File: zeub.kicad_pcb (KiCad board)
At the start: 2 copper layers, 94.5 x 62.2 mm, 227 parts, among them J1 debug-port, J2 OLED-128x64, J3 USB_C_Receptacle_USB2.0, Q1 AO3401A, Q2 AO3401A, Q3 AO3401A, Q4 AO3401A, SW1 SKRHA, SW2 RotaryEncoder_Switch, U1 IS31FL3729, U10 LTC4054ES5-4.2, U2 IS31FL3729, U3 IS31FL3729, U4 IS31FL3729, U5 holyiot-18010-no-underside, U6 MT25QL128ABA1ESE, U7 MC78M05_TO252, U8 XC6206PxxxMR, U9 SRV05-4

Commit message: routed RGB
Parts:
- moved D1 20.6 mm to (95.0, 20.0)
- moved D10 20.6 mm to (100.0, 25.0)
- moved D100 20.6 mm to (155.0, 35.0)
- moved D101 20.6 mm to (155.0, 40.0)
- moved D102 20.6 mm to (155.0, 45.0)
- moved D103 20.6 mm to (155.0, 50.0)
- moved D104 20.6 mm to (155.0, 55.0)
- moved D105 20.6 mm to (160.0, 20.0)
- moved D106 20.6 mm to (160.0, 25.0)
- moved D107 20.6 mm to (160.0, 30.0)
- moved D108 20.6 mm to (160.0, 35.0)
- moved D109 20.6 mm to (160.0, 40.0)
- moved D11 20.6 mm to (100.0, 30.0)
- moved D110 20.6 mm to (160.0, 45.0)
- moved D111 20.6 mm to (160.0, 50.0)
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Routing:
- net /led/RGB_G7: track 0.00 -> 44.7 mm, vias 0 -> 8
- net /led/RGB_G6: track 0.00 -> 44.7 mm, vias 0 -> 8
- net /led/RGB_G5: track 0.00 -> 44.7 mm, vias 0 -> 8
- net /led/RGB_G4: track 0.00 -> 44.7 mm, vias 0 -> 8
- net /led/RGB_G3: track 0.00 -> 44.7 mm, vias 0 -> 8
- net /led/RGB_G2: track 0.00 -> 44.7 mm, vias 0 -> 8
- net /led/RGB_G1: track 0.00 -> 44.7 mm, vias 0 -> 8
- net /led/RGB_G0: track 0.00 -> 44.7 mm, vias 0 -> 8
- net /led/RGB_C7: track 0.00 -> 44.2 mm
- net /led/RGB_C6: track 0.00 -> 44.2 mm
- net /led/RGB_C5: track 0.00 -> 44.2 mm
- net /led/RGB_C4: track 0.00 -> 44.2 mm
- net /led/RGB_C3: track 0.00 -> 44.2 mm
- net /led/RGB_C2: track 0.00 -> 44.2 mm
- net /led/RGB_C1: track 0.00 -> 44.2 mm
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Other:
- board outline removed

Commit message: routed matrix + PWM driver
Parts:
- added D197: white, Diode_SMD:D_0603_1608Metric, F.Cu at (128.0, 16.0)
- added D198: white, Diode_SMD:D_0603_1608Metric, F.Cu at (128.0, 20.0)
- added D199: white, Diode_SMD:D_0603_1608Metric, F.Cu at (128.0, 24.0)
- added D200: white, Diode_SMD:D_0603_1608Metric, F.Cu at (128.0, 28.0)
- added D201: white, Diode_SMD:D_0603_1608Metric, F.Cu at (132.0, 0.00)
- added D202: white, Diode_SMD:D_0603_1608Metric, F.Cu at (132.0, 4.00)
- added D203: white, Diode_SMD:D_0603_1608Metric, F.Cu at (132.0, 8.00)
- added D204: white, Diode_SMD:D_0603_1608Metric, F.Cu at (132.0, 12.0)
- added D205: white, Diode_SMD:D_0603_1608Metric, F.Cu at (132.0, 16.0)
- added D206: white, Diode_SMD:D_0603_1608Metric, F.Cu at (132.0, 20.0)
- added D207: white, Diode_SMD:D_0603_1608Metric, F.Cu at (132.0, 24.0)
- added D208: white, Diode_SMD:D_0603_1608Metric, F.Cu at (132.0, 28.0)
- added D209: white, Diode_SMD:D_0603_1608Metric, F.Cu at (136.0, 0.00)
- added D210: white, Diode_SMD:D_0603_1608Metric, F.Cu at (136.0, 4.00)
- added D211: white, Diode_SMD:D_0603_1608Metric, F.Cu at (136.0, 8.00)
- added D212: white, Diode_SMD:D_0603_1608Metric, F.Cu at (136.0, 12.0)
- added D213: white, Diode_SMD:D_0603_1608Metric, F.Cu at (136.0, 16.0)
- added D214: white, Diode_SMD:D_0603_1608Metric, F.Cu at (136.0, 20.0)
- added D215: white, Diode_SMD:D_0603_1608Metric, F.Cu at (136.0, 24.0)
- added D216: white, Diode_SMD:D_0603_1608Metric, F.Cu at (136.0, 28.0)
- added D217: white, Diode_SMD:D_0603_1608Metric, F.Cu at (140.0, 0.00)
- added D218: white, Diode_SMD:D_0603_1608Metric, F.Cu at (140.0, 4.00)
- added D219: white, Diode_SMD:D_0603_1608Metric, F.Cu at (140.0, 8.00)
- added D220: white, Diode_SMD:D_0603_1608Metric, F.Cu at (140.0, 12.0)
- added D221: white, Diode_SMD:D_0603_1608Metric, F.Cu at (140.0, 16.0)
- added D222: white, Diode_SMD:D_0603_1608Metric, F.Cu at (140.0, 20.0)
- added D223: white, Diode_SMD:D_0603_1608Metric, F.Cu at (140.0, 24.0)
- added D224: white, Diode_SMD:D_0603_1608Metric, F.Cu at (140.0, 28.0)
- added D225: white, Diode_SMD:D_0603_1608Metric, F.Cu at (144.0, 0.00)
- added D226: white, Diode_SMD:D_0603_1608Metric, F.Cu at (144.0, 4.00)
- added D227: white, Diode_SMD:D_0603_1608Metric, F.Cu at (144.0, 8.00)
- added D228: white, Diode_SMD:D_0603_1608Metric, F.Cu at (144.0, 12.0)
- added D229: white, Diode_SMD:D_0603_1608Metric, F.Cu at (144.0, 16.0)
- added D230: white, Diode_SMD:D_0603_1608Metric, F.Cu at (144.0, 20.0)
- added D231: white, Diode_SMD:D_0603_1608Metric, F.Cu at (144.0, 24.0)
- added D232: white, Diode_SMD:D_0603_1608Metric, F.Cu at (144.0, 28.0)
- added D233: white, Diode_SMD:D_0603_1608Metric, F.Cu at (148.0, 0.00)
- added D234: white, Diode_SMD:D_0603_1608Metric, F.Cu at (148.0, 4.00)
- added D235: white, Diode_SMD:D_0603_1608Metric, F.Cu at (148.0, 8.00)
- added D236: white, Diode_SMD:D_0603_1608Metric, F.Cu at (148.0, 12.0)
- added D237: white, Diode_SMD:D_0603_1608Metric, F.Cu at (148.0, 16.0)
- added D238: white, Diode_SMD:D_0603_1608Metric, F.Cu at (148.0, 20.0)
- added D239: white, Diode_SMD:D_0603_1608Metric, F.Cu at (148.0, 24.0)
- added D240: white, Diode_SMD:D_0603_1608Metric, F.Cu at (148.0, 28.0)
- added D241: white, Diode_SMD:D_0603_1608Metric, F.Cu at (152.0, 0.00)
- added D242: white, Diode_SMD:D_0603_1608Metric, F.Cu at (152.0, 4.00)
- added D243: white, Diode_SMD:D_0603_1608Metric, F.Cu at (152.0, 8.00)
- added D244: white, Diode_SMD:D_0603_1608Metric, F.Cu at (152.0, 12.0)
- added D245: white, Diode_SMD:D_0603_1608Metric, F.Cu at (152.0, 16.0)
- added D246: white, Diode_SMD:D_0603_1608Metric, F.Cu at (152.0, 20.0)
- added D247: white, Diode_SMD:D_0603_1608Metric, F.Cu at (152.0, 24.0)
- added D248: white, Diode_SMD:D_0603_1608Metric, F.Cu at (152.0, 28.0)
- added D249: white, Diode_SMD:D_0603_1608Metric, F.Cu at (156.0, 0.00)
- added D250: white, Diode_SMD:D_0603_1608Metric, F.Cu at (156.0, 4.00)
- added D251: white, Diode_SMD:D_0603_1608Metric, F.Cu at (156.0, 8.00)
- added D252: white, Diode_SMD:D_0603_1608Metric, F.Cu at (156.0, 12.0)
- added D253: white, Diode_SMD:D_0603_1608Metric, F.Cu at (156.0, 16.0)
- added D254: white, Diode_SMD:D_0603_1608Metric, F.Cu at (156.0, 20.0)
- added D255: white, Diode_SMD:D_0603_1608Metric, F.Cu at (156.0, 24.0)
- added D256: white, Diode_SMD:D_0603_1608Metric, F.Cu at (156.0, 28.0)
- added D257: LED_RABG, LED_SMD:LED_ASMB-KTF0-0A306, F.Cu at (0.00, 0.00)
- added D258: LED_RABG, LED_SMD:LED_ASMB-KTF0-0A306, F.Cu at (0.00, 4.00)
- added D259: LED_RABG, LED_SMD:LED_ASMB-KTF0-0A306, F.Cu at (0.00, 8.00)
- added D260: LED_RABG, LED_SMD:LED_ASMB-KTF0-0A306, F.Cu at (0.00, 12.0)
- added D261: LED_RABG, LED_SMD:LED_ASMB-KTF0-0A306, F.Cu at (0.00, 16.0)
- added D262: LED_RABG, LED_SMD:LED_ASMB-KTF0-0A306, F.Cu at (0.00, 20.0)
- added D263: LED_RABG, LED_SMD:LED_ASMB-KTF0-0A306, F.Cu at (0.00, 24.0)
- added D264: LED_RABG, LED_SMD:LED_ASMB-KTF0-0A306, F.Cu at (0.00, 28.0)
- added D265: LED_RABG, LED_SMD:LED_ASMB-KTF0-0A306, F.Cu at (4.00, 0.00)
- added D266: LED_RABG, LED_SMD:LED_ASMB-KTF0-0A306, F.Cu at (4.00, 4.00)
- added D267: LED_RABG, LED_SMD:LED_ASMB-KTF0-0A306, F.Cu at (4.00, 8.00)
- added D268: LED_RABG, LED_SMD:LED_ASMB-KTF0-0A306, F.Cu at (4.00, 12.0)
- added D269: LED_RABG, LED_SMD:LED_ASMB-KTF0-0A306, F.Cu at (4.00, 16.0)
- added D270: LED_RABG, LED_SMD:LED_ASMB-KTF0-0A306, F.Cu at (4.00, 20.0)
- added D271: LED_RABG, LED_SMD:LED_ASMB-KTF0-0A306, F.Cu at (4.00, 24.0)
- added D272: LED_RABG, LED_SMD:LED_ASMB-KTF0-0A306, F.Cu at (4.00, 28.0)
- added D273: LED_RABG, LED_SMD:LED_ASMB-KTF0-0A306, F.Cu at (8.00, 0.00)
- added D274: LED_RABG, LED_SMD:LED_ASMB-KTF0-0A306, F.Cu at (8.00, 4.00)
- added D275: LED_RABG, LED_SMD:LED_ASMB-KTF0-0A306, F.Cu at (8.00, 8.00)
- added D276: LED_RABG, LED_SMD:LED_ASMB-KTF0-0A306, F.Cu at (8.00, 12.0)
- added D277: LED_RABG, LED_SMD:LED_ASMB-KTF0-0A306, F.Cu at (8.00, 16.0)
- added D278: LED_RABG, LED_SMD:LED_ASMB-KTF0-0A306, F.Cu at (8.00, 20.0)
- added D279: LED_RABG, LED_SMD:LED_ASMB-KTF0-0A306, F.Cu at (8.00, 24.0)
- added D280: LED_RABG, LED_SMD:LED_ASMB-KTF0-0A306, F.Cu at (8.00, 28.0)
- added D281: LED_RABG, LED_SMD:LED_ASMB-KTF0-0A306, F.Cu at (12.0, 0.00)
- added D282: LED_RABG, LED_SMD:LED_ASMB-KTF0-0A306, F.Cu at (12.0, 4.00)
- added D283: LED_RABG, LED_SMD:LED_ASMB-KTF0-0A306, F.Cu at (12.0, 8.00)
- added D284: LED_RABG, LED_SMD:LED_ASMB-KTF0-0A306, F.Cu at (12.0, 12.0)
- added D285: LED_RABG, LED_SMD:LED_ASMB-KTF0-0A306, F.Cu at (12.0, 16.0)
- added D286: LED_RABG, LED_SMD:LED_ASMB-KTF0-0A306, F.Cu at (12.0, 20.0)
- added D287: LED_RABG, LED_SMD:LED_ASMB-KTF0-0A306, F.Cu at (12.0, 24.0)
- added D288: LED_RABG, LED_SMD:LED_ASMB-KTF0-0A306, F.Cu at (12.0, 28.0)
- added D289: LED_RABG, LED_SMD:LED_ASMB-KTF0-0A306, F.Cu at (16.0, 0.00)
- added D290: LED_RABG, LED_SMD:LED_ASMB-KTF0-0A306, F.Cu at (16.0, 4.00)
- added D291: LED_RABG, LED_SMD:LED_ASMB-KTF0-0A306, F.Cu at (16.0, 8.00)
- added D292: LED_RABG, LED_SMD:LED_ASMB-KTF0-0A306, F.Cu at (16.0, 12.0)
- added D293: LED_RABG, LED_SMD:LED_ASMB-KTF0-0A306, F.Cu at (16.0, 16.0)
- added D294: LED_RABG, LED_SMD:LED_ASMB-KTF0-0A306, F.Cu at (16.0, 20.0)
- added D295: LED_RABG, LED_SMD:LED_ASMB-KTF0-0A306, F.Cu at (16.0, 24.0)
- added D296: LED_RABG, LED_SMD:LED_ASMB-KTF0-0A306, F.Cu at (16.0, 28.0)
- added D297: LED_RABG, LED_SMD:LED_ASMB-KTF0-0A306, F.Cu at (20.0, 0.00)
- added D298: LED_RABG, LED_SMD:LED_ASMB-KTF0-0A306, F.Cu at (20.0, 4.00)
- added D299: LED_RABG, LED_SMD:LED_ASMB-KTF0-0A306, F.Cu at (20.0, 8.00)
- added D300: LED_RABG, LED_SMD:LED_ASMB-KTF0-0A306, F.Cu at (20.0, 12.0)
- added D301: LED_RABG, LED_SMD:LED_ASMB-KTF0-0A306, F.Cu at (20.0, 16.0)
- added D302: LED_RABG, LED_SMD:LED_ASMB-KTF0-0A306, F.Cu at (20.0, 20.0)
- added D303: LED_RABG, LED_SMD:LED_ASMB-KTF0-0A306, F.Cu at (20.0, 24.0)
- added D304: LED_RABG, LED_SMD:LED_ASMB-KTF0-0A306, F.Cu at (20.0, 28.0)
- added D305: LED_RABG, LED_SMD:LED_ASMB-KTF0-0A306, F.Cu at (24.0, 0.00)
- added D306: LED_RABG, LED_SMD:LED_ASMB-KTF0-0A306, F.Cu at (24.0, 4.00)
- added D307: LED_RABG, LED_SMD:LED_ASMB-KTF0-0A306, F.Cu at (24.0, 8.00)
- added D308: LED_RABG, LED_SMD:LED_ASMB-KTF0-0A306, F.Cu at (24.0, 12.0)
- added D309: LED_RABG, LED_SMD:LED_ASMB-KTF0-0A306, F.Cu at (24.0, 16.0)
- added D310: LED_RABG, LED_SMD:LED_ASMB-KTF0-0A306, F.Cu at (24.0, 20.0)
- added D311: LED_RABG, LED_SMD:LED_ASMB-KTF0-0A306, F.Cu at (24.0, 24.0)
- added D312: LED_RABG, LED_SMD:LED_ASMB-KTF0-0A306, F.Cu at (24.0, 28.0)
- added D313: LED_RABG, LED_SMD:LED_ASMB-KTF0-0A306, F.Cu at (28.0, 0.00)
- added D314: LED_RABG, LED_SMD:LED_ASMB-KTF0-0A306, F.Cu at (28.0, 4.00)
- added D315: LED_RABG, LED_SMD:LED_ASMB-KTF0-0A306, F.Cu at (28.0, 8.00)
- added D316: LED_RABG, LED_SMD:LED_ASMB-KTF0-0A306, F.Cu at (28.0, 12.0)
- added D317: LED_RABG, LED_SMD:LED_ASMB-KTF0-0A306, F.Cu at (28.0, 16.0)
- added D318: LED_RABG, LED_SMD:LED_ASMB-KTF0-0A306, F.Cu at (28.0, 20.0)
- added D319: LED_RABG, LED_SMD:LED_ASMB-KTF0-0A306, F.Cu at (28.0, 24.0)
- added D320: LED_RABG, LED_SMD:LED_ASMB-KTF0-0A306, F.Cu at (28.0, 28.0)
- added D321: D_Schottky, Diode_SMD:D_SOD-123, B.Cu at (-19.0, 58.8)
- added D322: D_Schottky, Diode_SMD:D_SOD-123, B.Cu at (-13.2, 62.1)
- added D323: D_Schottky, Diode_SMD:D_SOD-123, B.Cu at (-13.2, 58.8)
- added D324: LED, Diode_SMD:D_0805_2012Metric, B.Cu at (-18.4, 61.9)
- added J4: Barrel_Jack_Switch, Connector_BarrelJack:BarrelJack_CUI_PJ-102AH_Horizontal, B.Cu at (-5.05, 3.50)
- added J5: Conn_01x03, Connector_PinHeader_2.54mm:PinHeader_1x03_P2.54mm_Vertical, F.Cu at (-16.8, 21.7)
- added J6: Conn_01x03, Connector_PinHeader_2.54mm:PinHeader_1x03_P2.54mm_Vertical, F.Cu at (-16.8, 11.7)
- added Q5: AO3401A, Package_TO_SOT_SMD:SOT-23, B.Cu at (-33.5, 49.2)
- added R13: 10k, Resistor_SMD:R_0603_1608Metric, B.Cu at (55.0, 39.2)
- added R14: 10k, Resistor_SMD:R_0603_1608Metric, B.Cu at (116.7, 45.5)
- added R15: 10k, Resistor_SMD:R_0603_1608Metric, B.Cu at (3.50, 38.0)
- added R16: 10k, Resistor_SMD:R_0603_1608Metric, B.Cu at (20.2, 40.0)
- added R17: 20, Resistor_SMD:R_0603_1608Metric, F.Cu at (31.5, 31.2)
- added R18: 20, Resistor_SMD:R_0603_1608Metric, F.Cu at (35.2, 31.2)
- added R19: 20, Resistor_SMD:R_0603_1608Metric, F.Cu at (39.2, 31.2)
- added R20: 20, Resistor_SMD:R_0603_1608Metric, F.Cu at (43.2, 31.2)
- added R21: 20, Resistor_SMD:R_0603_1608Metric, F.Cu at (47.2, 31.2)
- added R22: 20, Resistor_SMD:R_0603_1608Metric, F.Cu at (51.2, 31.2)
- added R23: 20, Resistor_SMD:R_0603_1608Metric, F.Cu at (55.2, 31.2)
- added R24: 20, Resistor_SMD:R_0603_1608Metric, F.Cu at (59.2, 31.2)
- added R25: 20, Resistor_SMD:R_0603_1608Metric, F.Cu at (63.2, 31.2)
- added R26: 20, Resistor_SMD:R_0603_1608Metric, F.Cu at (67.2, 31.2)
- added R27: 20, Resistor_SMD:R_0603_1608Metric, F.Cu at (71.2, 31.2)
- added R28: 20, Resistor_SMD:R_0603_1608Metric, F.Cu at (75.2, 31.2)
- added R29: 20, Resistor_SMD:R_0603_1608Metric, F.Cu at (79.2, 31.2)
- added R30: 20, Resistor_SMD:R_0603_1608Metric, F.Cu at (83.2, 31.2)
- added R31: 20, Resistor_SMD:R_0603_1608Metric, F.Cu at (87.2, 31.2)
- added R32: 20, Resistor_SMD:R_0603_1608Metric, F.Cu at (91.2, 31.2)
- added R33: 20, Resistor_SMD:R_0603_1608Metric, F.Cu at (95.2, 31.2)
- added R34: 20, Resistor_SMD:R_0603_1608Metric, F.Cu at (99.2, 31.2)
- added R35: 20, Resistor_SMD:R_0603_1608Metric, F.Cu at (103.2, 31.2)
- added R36: 20, Resistor_SMD:R_0603_1608Metric, F.Cu at (107.2, 31.2)
- added R37: 20, Resistor_SMD:R_0603_1608Metric, F.Cu at (111.2, 31.2)
- added R38: 20, Resistor_SMD:R_0603_1608Metric, F.Cu at (115.2, 31.2)
- added R39: 20, Resistor_SMD:R_0603_1608Metric, F.Cu at (119.2, 31.2)
- added R40: 20, Resistor_SMD:R_0603_1608Metric, F.Cu at (123.2, 31.2)
- added R41: 20, Resistor_SMD:R_0603_1608Metric, F.Cu at (127.2, 31.2)
- added R42: 20, Resistor_SMD:R_0603_1608Metric, F.Cu at (131.2, 31.2)
- added R43: 20, Resistor_SMD:R_0603_1608Metric, F.Cu at (135.2, 31.2)
- added R44: 20, Resistor_SMD:R_0603_1608Metric, F.Cu at (139.2, 31.2)
- added R45: 20, Resistor_SMD:R_0603_1608Metric, F.Cu at (143.2, 31.2)
- added R46: 20, Resistor_SMD:R_0603_1608Metric, F.Cu at (147.2, 31.2)
- added R47: 20, Resistor_SMD:R_0603_1608Metric, F.Cu at (151.2, 31.2)
- added R48: 20, Resistor_SMD:R_0603_1608Metric, F.Cu at (155.2, 31.2)
- added R49: 20, Resistor_SMD:R_0603_1608Metric, B.Cu at (-0.75, 28.2)
- added R50: 20, Resistor_SMD:R_0603_1608Metric, B.Cu at (0.75, 28.2)
- added R51: 20, Resistor_SMD:R_0603_1608Metric, B.Cu at (2.00, 31.2)
- added R52: 20, Resistor_SMD:R_0603_1608Metric, B.Cu at (3.25, 28.2)
- added R53: 20, Resistor_SMD:R_0603_1608Metric, B.Cu at (4.75, 28.2)
- added R54: 20, Resistor_SMD:R_0603_1608Metric, B.Cu at (6.00, 31.2)
- added R55: 20, Resistor_SMD:R_0603_1608Metric, B.Cu at (7.25, 28.2)
- added R56: 20, Resistor_SMD:R_0603_1608Metric, B.Cu at (8.75, 28.2)
- added R57: 20, Resistor_SMD:R_0603_1608Metric, B.Cu at (10.0, 31.2)
- added R58: 20, Resistor_SMD:R_0603_1608Metric, B.Cu at (11.2, 28.2)
- added R59: 20, Resistor_SMD:R_0603_1608Metric, B.Cu at (12.8, 28.2)
- added R60: 20, Resistor_SMD:R_0603_1608Metric, B.Cu at (14.0, 31.2)
- added R61: 20, Resistor_SMD:R_0603_1608Metric, B.Cu at (15.2, 28.2)
- added R62: 20, Resistor_SMD:R_0603_1608Metric, B.Cu at (16.8, 28.2)
- added R63: 20, Resistor_SMD:R_0603_1608Metric, B.Cu at (18.0, 31.2)
- added R64: 20, Resistor_SMD:R_0603_1608Metric, B.Cu at (19.2, 28.2)
- added R65: 20, Resistor_SMD:R_0603_1608Metric, B.Cu at (20.8, 28.2)
- added R66: 20, Resistor_SMD:R_0603_1608Metric, B.Cu at (22.0, 31.2)
- added R67: 20, Resistor_SMD:R_0603_1608Metric, B.Cu at (23.2, 28.2)
- added R68: 20, Resistor_SMD:R_0603_1608Metric, B.Cu at (24.8, 28.2)
- added R69: 20, Resistor_SMD:R_0603_1608Metric, B.Cu at (26.0, 31.2)
- added R70: 20, Resistor_SMD:R_0603_1608Metric, B.Cu at (27.2, 28.2)
- added R71: 20, Resistor_SMD:R_0603_1608Metric, B.Cu at (28.8, 28.2)
- added R72: 20, Resistor_SMD:R_0603_1608Metric, B.Cu at (30.0, 31.2)
- added R73: 100k, Resistor_SMD:R_0603_1608Metric, B.Cu at (-37.9, 48.3)
- D129, D130, D131, D132, D133, D134, D135, D136, D137, D138, D139, D140, D141, D142, D143, D144, D145, D146, D147, D148, D149, D150, D151, D152, D153, D154, D155, D156, D157, D158, D159, D160, D161, D162, D163, D164, D165, D166, D167, D168, D169, D170, D171, D172, D173, D174, D175, D176, D177, D178, D179, D180, D181, D182, D183, D184, D185, D186, D187, D188, D189, D190, D191, D192: value LED_RABG -> white; footprint LED_SMD:LED_ASMB-KTF0-0A306 -> Diode_SMD:D_0603_1608Metric
- D193, D194, D195: value D_Schottky -> white; footprint Diode_SMD:D_SOD-123 -> Diode_SMD:D_0603_1608Metric
- D196: value LED -> white; footprint Diode_SMD:D_0805_2012Metric -> Diode_SMD:D_0603_1608Metric
- J2: value OLED-128x64 -> OLED-128x32; footprint display:OLED-128x64 -> display:OLED-128x32-cutout
- J3, Q1, Q2, Q3, Q4, R1, R10, R11, R12, R2, R3, R4, R5, R6, R7, R8, R9, U1, U10, U2, U3, U4, U5, U6, U7, U8, U9: moved to B.Cu
- moved R11 353.0 mm to (-59.8, 27.0), turned to 180 degrees
- moved R9 340.5 mm to (-53.5, 33.3), turned to 180 degrees
- moved U9 331.5 mm to (-48.9, 31.3), turned to 180 degrees
- moved U10 330.6 mm to (-48.4, 36.0), turned to 180 degrees
- moved R12 329.5 mm to (-47.8, 39.5), turned to 180 degrees
- moved R10 317.8 mm to (-41.9, 45.5), turned to 180 degrees
- moved U7 314.5 mm to (-40.2, 29.7), turned to 180 degrees
- moved U8 308.9 mm to (-36.2, 41.2), turned to 180 degrees
- moved J3 287.7 mm to (-15.0, 49.2), turned to 90 degrees
- moved R6 275.7 mm to (-13.5, 15.5), turned to 180 degrees
- moved R5 267.0 mm to (-13.5, 10.5), turned to 180 degrees
- moved R3 263.6 mm to (-7.50, 22.0), turned to 180 degrees
- moved R1 263.0 mm to (-7.50, 12.0), turned to 180 degrees
- moved R7 259.8 mm to (-13.5, 20.5), turned to 180 degrees
- moved R8 256.4 mm to (-13.5, 25.5), turned to 180 degrees
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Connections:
- D129 pad 1: /led/RGB_R0 -> /led/W_C16
- D129 pad 2: /led/RGB_C0 -> /led/W_R0
- D130 pad 1: /led/RGB_R0 -> /led/W_C16
- D130 pad 2: /led/RGB_C1 -> /led/W_R1
- D131 pad 1: /led/RGB_R0 -> /led/W_C16
- D131 pad 2: /led/RGB_C2 -> /led/W_R2
- D132 pad 1: /led/RGB_R0 -> /led/W_C16
- D132 pad 2: /led/RGB_C3 -> /led/W_R3
- D133 pad 1: /led/RGB_R0 -> /led/W_C16
- D133 pad 2: /led/RGB_C4 -> /led/W_R4
- D134 pad 1: /led/RGB_R0 -> /led/W_C16
- D134 pad 2: /led/RGB_C5 -> /led/W_R5
- D135 pad 1: /led/RGB_R0 -> /led/W_C16
- D135 pad 2: /led/RGB_C6 -> /led/W_R6
- D136 pad 1: /led/RGB_R0 -> /led/W_C16
- D136 pad 2: /led/RGB_C7 -> /led/W_R7
- D137 pad 1: /led/RGB_R1 -> /led/W_C17
- D137 pad 2: /led/RGB_C0 -> /led/W_R0
- D138 pad 1: /led/RGB_R1 -> /led/W_C17
- D138 pad 2: /led/RGB_C1 -> /led/W_R1
- D139 pad 1: /led/RGB_R1 -> /led/W_C17
- D139 pad 2: /led/RGB_C2 -> /led/W_R2
- D140 pad 1: /led/RGB_R1 -> /led/W_C17
- D140 pad 2: /led/RGB_C3 -> /led/W_R3
- D141 pad 1: /led/RGB_R1 -> /led/W_C17
- D141 pad 2: /led/RGB_C4 -> /led/W_R4
- D142 pad 1: /led/RGB_R1 -> /led/W_C17
- D142 pad 2: /led/RGB_C5 -> /led/W_R5
- D143 pad 1: /led/RGB_R1 -> /led/W_C17
- D143 pad 2: /led/RGB_C6 -> /led/W_R6
- D144 pad 1: /led/RGB_R1 -> /led/W_C17
- D144 pad 2: /led/RGB_C7 -> /led/W_R7
- D145 pad 1: /led/RGB_R2 -> /led/W_C18
- D145 pad 2: /led/RGB_C0 -> /led/W_R0
- D146 pad 1: /led/RGB_R2 -> /led/W_C18
- D146 pad 2: /led/RGB_C1 -> /led/W_R1
- D147 pad 1: /led/RGB_R2 -> /led/W_C18
- D147 pad 2: /led/RGB_C2 -> /led/W_R2
- D148 pad 1: /led/RGB_R2 -> /led/W_C18
- D148 pad 2: /led/RGB_C3 -> /led/W_R3
- D149 pad 1: /led/RGB_R2 -> /led/W_C18
- D149 pad 2: /led/RGB_C4 -> /led/W_R4
- D150 pad 1: /led/RGB_R2 -> /led/W_C18
- D150 pad 2: /led/RGB_C5 -> /led/W_R5
- D151 pad 1: /led/RGB_R2 -> /led/W_C18
- D151 pad 2: /led/RGB_C6 -> /led/W_R6
- D152 pad 1: /led/RGB_R2 -> /led/W_C18
- D152 pad 2: /led/RGB_C7 -> /led/W_R7
- D153 pad 1: /led/RGB_R3 -> /led/W_C19
- D153 pad 2: /led/RGB_C0 -> /led/W_R0
- D154 pad 1: /led/RGB_R3 -> /led/W_C19
- D154 pad 2: /led/RGB_C1 -> /led/W_R1
- D155 pad 1: /led/RGB_R3 -> /led/W_C19
- D155 pad 2: /led/RGB_C2 -> /led/W_R2
- D156 pad 1: /led/RGB_R3 -> /led/W_C19
- D156 pad 2: /led/RGB_C3 -> /led/W_R3
- D157 pad 1: /led/RGB_R3 -> /led/W_C19
- D157 pad 2: /led/RGB_C4 -> /led/W_R4
- D158 pad 1: /led/RGB_R3 -> /led/W_C19
- D158 pad 2: /led/RGB_C5 -> /led/W_R5
- D159 pad 1: /led/RGB_R3 -> /led/W_C19
- D159 pad 2: /led/RGB_C6 -> /led/W_R6
- D160 pad 1: /led/RGB_R3 -> /led/W_C19
- D160 pad 2: /led/RGB_C7 -> /led/W_R7
- D161 pad 1: /led/RGB_R4 -> /led/W_C20
- D161 pad 2: /led/RGB_C0 -> /led/W_R0
- D162 pad 1: /led/RGB_R4 -> /led/W_C20
- D162 pad 2: /led/RGB_C1 -> /led/W_R1
- D163 pad 1: /led/RGB_R4 -> /led/W_C20
- D163 pad 2: /led/RGB_C2 -> /led/W_R2
- D164 pad 1: /led/RGB_R4 -> /led/W_C20
- D164 pad 2: /led/RGB_C3 -> /led/W_R3
- D165 pad 1: /led/RGB_R4 -> /led/W_C20
- D165 pad 2: /led/RGB_C4 -> /led/W_R4
- D166 pad 1: /led/RGB_R4 -> /led/W_C20
- D166 pad 2: /led/RGB_C5 -> /led/W_R5
- D167 pad 1: /led/RGB_R4 -> /led/W_C20
- D167 pad 2: /led/RGB_C6 -> /led/W_R6
- D168 pad 1: /led/RGB_R4 -> /led/W_C20
- D168 pad 2: /led/RGB_C7 -> /led/W_R7
- D169 pad 1: /led/RGB_R5 -> /led/W_C21
- D169 pad 2: /led/RGB_C0 -> /led/W_R0
- D170 pad 1: /led/RGB_R5 -> /led/W_C21
- D170 pad 2: /led/RGB_C1 -> /led/W_R1
- D171 pad 1: /led/RGB_R5 -> /led/W_C21
- D171 pad 2: /led/RGB_C2 -> /led/W_R2
- D172 pad 1: /led/RGB_R5 -> /led/W_C21
- D172 pad 2: /led/RGB_C3 -> /led/W_R3
- D173 pad 1: /led/RGB_R5 -> /led/W_C21
- D173 pad 2: /led/RGB_C4 -> /led/W_R4
- D174 pad 1: /led/RGB_R5 -> /led/W_C21
- D174 pad 2: /led/RGB_C5 -> /led/W_R5
- D175 pad 1: /led/RGB_R5 -> /led/W_C21
- D175 pad 2: /led/RGB_C6 -> /led/W_R6
- D176 pad 1: /led/RGB_R5 -> /led/W_C21
- D176 pad 2: /led/RGB_C7 -> /led/W_R7
- D177 pad 1: /led/RGB_R6 -> /led/W_C22
- D177 pad 2: /led/RGB_C0 -> /led/W_R0
- D178 pad 1: /led/RGB_R6 -> /led/W_C22
- D178 pad 2: /led/RGB_C1 -> /led/W_R1
- D179 pad 1: /led/RGB_R6 -> /led/W_C22
- D179 pad 2: /led/RGB_C2 -> /led/W_R2
- D180 pad 1: /led/RGB_R6 -> /led/W_C22
- D180 pad 2: /led/RGB_C3 -> /led/W_R3
- D181 pad 1: /led/RGB_R6 -> /led/W_C22
- D181 pad 2: /led/RGB_C4 -> /led/W_R4
- D182 pad 1: /led/RGB_R6 -> /led/W_C22
- D182 pad 2: /led/RGB_C5 -> /led/W_R5
- D183 pad 1: /led/RGB_R6 -> /led/W_C22
- D183 pad 2: /led/RGB_C6 -> /led/W_R6
- D184 pad 1: /led/RGB_R6 -> /led/W_C22
- D184 pad 2: /led/RGB_C7 -> /led/W_R7
- D185 pad 1: /led/RGB_R7 -> /led/W_C23
- D185 pad 2: /led/RGB_C0 -> /led/W_R0
- D186 pad 1: /led/RGB_R7 -> /led/W_C23
- D186 pad 2: /led/RGB_C1 -> /led/W_R1
- D187 pad 1: /led/RGB_R7 -> /led/W_C23
- D187 pad 2: /led/RGB_C2 -> /led/W_R2
- D188 pad 1: /led/RGB_R7 -> /led/W_C23
- D188 pad 2: /led/RGB_C3 -> /led/W_R3
- D189 pad 1: /led/RGB_R7 -> /led/W_C23
- D189 pad 2: /led/RGB_C4 -> /led/W_R4
- D190 pad 1: /led/RGB_R7 -> /led/W_C23
- D190 pad 2: /led/RGB_C5 -> /led/W_R5
- D191 pad 1: /led/RGB_R7 -> /led/W_C23
- D191 pad 2: /led/RGB_C6 -> /led/W_R6
- D192 pad 1: /led/RGB_R7 -> /led/W_C23
- D192 pad 2: /led/RGB_C7 -> /led/W_R7
- D193 pad 1: +5V -> /led/W_C24
- D193 pad 2: VBUS -> /led/W_R0
- D194 pad 1: +5V -> /led/W_C24
- D194 pad 2: +BATT -> /led/W_R1
- D195 pad 1: +5V -> /led/W_C24
- D195 pad 2: Net-(D195-Pad2) -> /led/W_R2
- D196 pad 1: Net-(D196-Pad1) -> /led/W_C24
- D196 pad 2: Net-(D196-Pad2) -> /led/W_R3
- R11 pad 2: Net-(D196-Pad2) -> Net-(D324-Pad2)
- R2 pad 1: PWMY1 -> PWMY0
- U1 pad 1: /led/W_C03 -> Net-(U1-Pad1)
- U1 pad 10: /led/W_C11 -> Net-(U1-Pad10)
- U1 pad 11: /led/W_C12 -> Net-(U1-Pad11)
- U1 pad 12: /led/W_C13 -> Net-(U1-Pad12)
- U1 pad 13: /led/W_C14 -> Net-(U1-Pad13)
- U1 pad 14: /led/W_C15 -> Net-(U1-Pad14)
- U1 pad 15: /led/W_R7 -> /led/W_R0
- U1 pad 16: /led/W_R6 -> /led/W_R1
- U1 pad 17: /led/W_R5 -> /led/W_R2
- U1 pad 18: /led/W_R4 -> /led/W_R3
- U1 pad 19: /led/W_R3 -> /led/W_R4
- U1 pad 2: /led/W_C04 -> Net-(U1-Pad2)
- U1 pad 20: /led/W_R2 -> /led/W_R5
- U1 pad 21: /led/W_R1 -> /led/W_R6
- U1 pad 22: /led/W_R0 -> /led/W_R7
- U1 pad 25: unconnected-(U1-Pad25) -> Net-(R13-Pad2)
- U1 pad 3: /led/W_C05 -> Net-(U1-Pad3)
- U1 pad 30: /led/W_C00 -> Net-(U1-Pad30)
- U1 pad 31: /led/W_C01 -> Net-(U1-Pad31)
- U1 pad 32: /led/W_C02 -> Net-(U1-Pad32)
- U1 pad 4: /led/W_C06 -> Net-(U1-Pad4)
- U1 pad 5: /led/W_C07 -> Net-(U1-Pad5)
- U1 pad 6: /led/W_C08 -> Net-(U1-Pad6)
- U1 pad 7: /led/W_C09 -> Net-(U1-Pad7)
- U1 pad 8: /led/W_C10 -> Net-(U1-Pad8)
- U10 pad 1: Net-(D196-Pad1) -> Net-(D324-Pad1)
- U2 pad 1: /led/W_C19 -> Net-(U2-Pad1)
- U2 pad 10: /led/W_C27 -> Net-(U2-Pad10)
- U2 pad 11: /led/W_C28 -> Net-(U2-Pad11)
- U2 pad 12: /led/W_C29 -> Net-(U2-Pad12)
- U2 pad 13: /led/W_C30 -> Net-(U2-Pad13)
- U2 pad 14: /led/W_C31 -> Net-(U2-Pad14)
- U2 pad 15: /led/W_R7 -> /led/W_R0
- U2 pad 16: /led/W_R6 -> /led/W_R1
- U2 pad 17: /led/W_R5 -> /led/W_R2
- U2 pad 18: /led/W_R4 -> /led/W_R3
- U2 pad 19: /led/W_R3 -> /led/W_R4
- U2 pad 2: /led/W_C20 -> Net-(U2-Pad2)
- U2 pad 20: /led/W_R2 -> /led/W_R5
- U2 pad 21: /led/W_R1 -> /led/W_R6
- U2 pad 22: /led/W_R0 -> /led/W_R7
- U2 pad 25: unconnected-(U2-Pad25) -> Net-(R14-Pad2)
- U2 pad 3: /led/W_C21 -> Net-(U2-Pad3)
- U2 pad 30: /led/W_C16 -> Net-(U2-Pad30)
- U2 pad 31: /led/W_C17 -> Net-(U2-Pad31)
- U2 pad 32: /led/W_C18 -> Net-(U2-Pad32)
- U2 pad 4: /led/W_C22 -> Net-(U2-Pad4)
- U2 pad 5: /led/W_C23 -> Net-(U2-Pad5)
- U2 pad 6: /led/W_C24 -> Net-(U2-Pad6)
- U2 pad 7: /led/W_C25 -> Net-(U2-Pad7)
- U2 pad 8: /led/W_C26 -> Net-(U2-Pad8)
- U3 pad 1: /led/RGB_R1 -> Net-(U3-Pad1)
- U3 pad 10: /led/RGB_B3 -> Net-(U3-Pad10)
- U3 pad 15: /led/RGB_C7 -> /led/RGB_C0
- U3 pad 16: /led/RGB_C6 -> /led/RGB_C1
- U3 pad 17: /led/RGB_C5 -> /led/RGB_C2
- U3 pad 18: /led/RGB_C4 -> /led/RGB_C3
- U3 pad 19: /led/RGB_C3 -> /led/RGB_C4
- U3 pad 2: /led/RGB_G1 -> Net-(U3-Pad2)
- U3 pad 20: /led/RGB_C2 -> /led/RGB_C5
- U3 pad 21: /led/RGB_C1 -> /led/RGB_C6
- U3 pad 22: /led/RGB_C0 -> /led/RGB_C7
- U3 pad 25: unconnected-(U3-Pad25) -> Net-(R15-Pad2)
- U3 pad 3: /led/RGB_B1 -> Net-(U3-Pad3)
- U3 pad 30: /led/RGB_R0 -> Net-(U3-Pad30)
- U3 pad 31: /led/RGB_G0 -> Net-(U3-Pad31)
- U3 pad 32: /led/RGB_B0 -> Net-(U3-Pad32)
- U3 pad 4: /led/RGB_R2 -> Net-(U3-Pad4)
- U3 pad 5: /led/RGB_G2 -> Net-(U3-Pad5)
- U3 pad 6: /led/RGB_B2 -> Net-(U3-Pad6)
- U3 pad 7: /led/RGB_R3 -> Net-(U3-Pad7)
- U3 pad 8: /led/RGB_G3 -> Net-(U3-Pad8)
- U4 pad 1: /led/RGB_R5 -> Net-(U4-Pad1)
- U4 pad 10: /led/RGB_B7 -> Net-(U4-Pad10)
- U4 pad 15: /led/RGB_C7 -> /led/RGB_C0
- U4 pad 16: /led/RGB_C6 -> /led/RGB_C1
- U4 pad 17: /led/RGB_C5 -> /led/RGB_C2
- U4 pad 18: /led/RGB_C4 -> /led/RGB_C3
- U4 pad 19: /led/RGB_C3 -> /led/RGB_C4
- U4 pad 2: /led/RGB_G5 -> Net-(U4-Pad2)
- U4 pad 20: /led/RGB_C2 -> /led/RGB_C5
- U4 pad 21: /led/RGB_C1 -> /led/RGB_C6
- U4 pad 22: /led/RGB_C0 -> /led/RGB_C7
- U4 pad 25: unconnected-(U4-Pad25) -> Net-(R16-Pad2)
- U4 pad 3: /led/RGB_B5 -> Net-(U4-Pad3)
- U4 pad 30: /led/RGB_R4 -> Net-(U4-Pad30)
- U4 pad 31: /led/RGB_G4 -> Net-(U4-Pad31)
- U4 pad 32: /led/RGB_B4 -> Net-(U4-Pad32)
- U4 pad 4: /led/RGB_R6 -> Net-(U4-Pad4)
- U4 pad 5: /led/RGB_G6 -> Net-(U4-Pad5)
- U4 pad 6: /led/RGB_B6 -> Net-(U4-Pad6)
- U4 pad 7: /led/RGB_R7 -> Net-(U4-Pad7)
- U4 pad 8: /led/RGB_G7 -> Net-(U4-Pad8)
- U5 pad 10: PWMY1 -> PWMY0
- U7 pad 3: Net-(D195-Pad2) -> Net-(D323-Pad2)
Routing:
- net /led/W_R7: track 96.4 -> 188.0 mm, vias 16 -> 0
- net /led/W_R6: track 96.4 -> 188.0 mm, vias 16 -> 0
- net /led/W_R5: track 96.4 -> 188.0 mm, vias 16 -> 0
- net /led/W_R4: track 96.4 -> 188.0 mm, vias 16 -> 0
- net /led/W_R3: track 96.4 -> 188.0 mm, vias 16 -> 0
- net /led/W_R2: track 96.4 -> 188.0 mm, vias 16 -> 0
- net /led/W_R1: track 96.4 -> 188.0 mm, vias 16 -> 0
- net /led/W_R0: track 96.4 -> 188.0 mm, vias 16 -> 0
- net +12V: track 0.00 -> 46.8 mm
- net /led/W_C28: track 0.00 -> 39.3 mm, vias 0 -> 8
- net /led/W_C23: track 0.00 -> 39.3 mm, vias 0 -> 8
- net /led/W_C17: track 0.00 -> 39.3 mm, vias 0 -> 8
- net /led/W_C31: track 0.00 -> 39.3 mm, vias 0 -> 8
- net /led/W_C30: track 0.00 -> 39.3 mm, vias 0 -> 8
- net /led/W_C29: track 0.00 -> 39.3 mm, vias 0 -> 8
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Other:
- board outline added: 177.8 x 60 mm

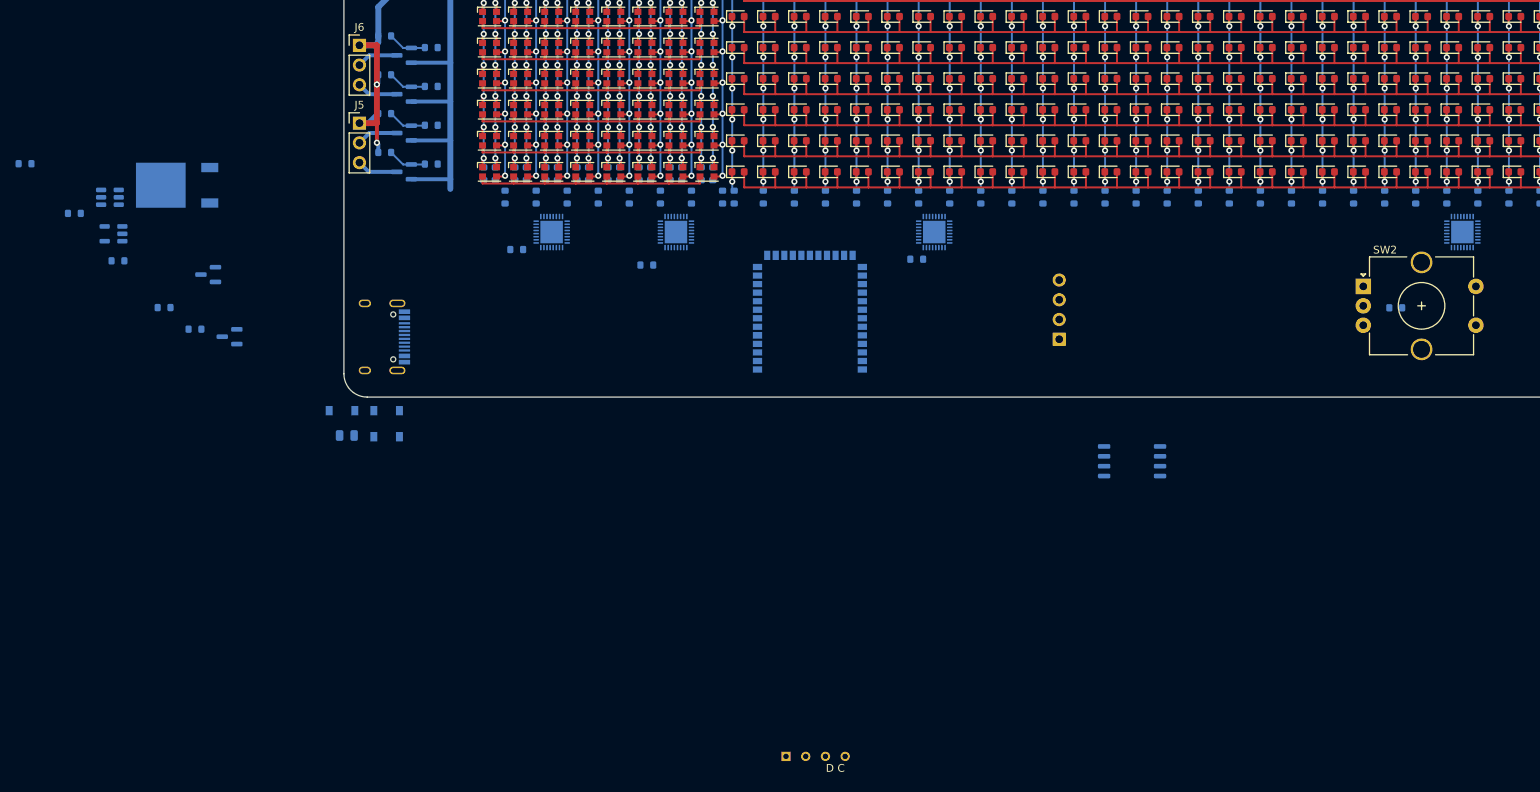
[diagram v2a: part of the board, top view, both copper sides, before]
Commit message: routed PMU
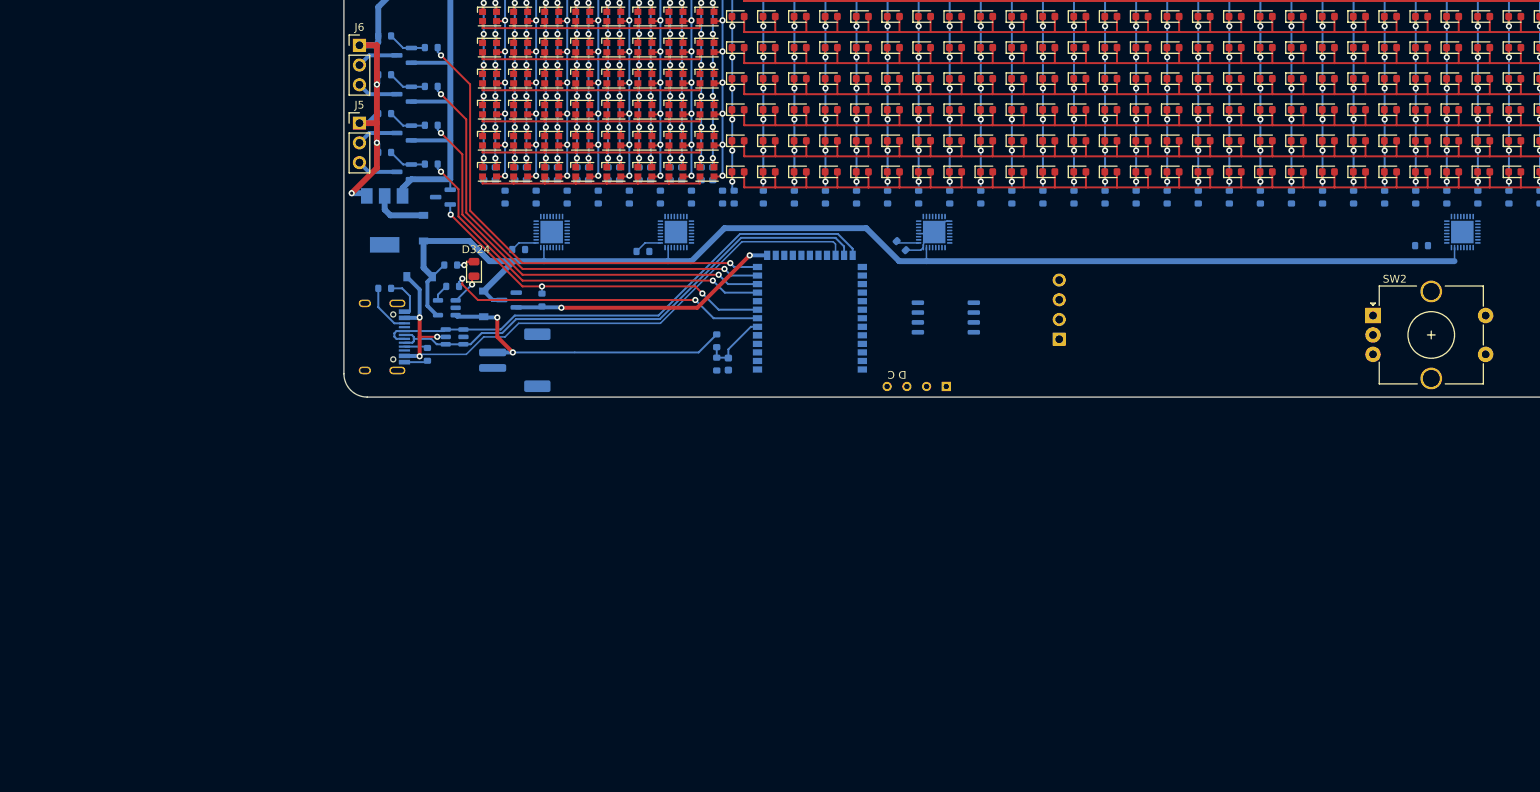
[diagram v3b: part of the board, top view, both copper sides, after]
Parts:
- added BT1: Battery_Cell, Connector_JST:JST_PH_S2B-PH-SM4-TB_1x02-1MP_P2.00mm_Horizontal, B.Cu at (3.25, 52.2)
- added C1: 10nF, Capacitor_SMD:C_0603_1608Metric, B.Cu at (30.8, 52.8)
- added R74: 5.1M, Resistor_SMD:R_0603_1608Metric, B.Cu at (29.2, 49.8)
- added R75: 5.1M, Resistor_SMD:R_0603_1608Metric, B.Cu at (29.2, 52.8)
- D324: moved to F.Cu
- R49, R52, R55, R58, R61, R64, R67, R70: value 20 -> 51
- U7: value MC78M05_TO252 -> TLV1117-50; footprint Package_TO_SOT_SMD:TO-252-2 -> Package_TO_SOT_SMD:SOT-223
- moved R11 56.3 mm to (-5.00, 40.0), turned to 0 degrees
- moved J1 49.4 mm to (55.0, 55.6), turned to 180 degrees
- moved R9 48.9 mm to (-8.00, 51.5), turned to 90 degrees
- moved U9 47.9 mm to (-4.50, 49.2)
- moved R73 44.8 mm to (6.75, 44.5), turned to 90 degrees
- moved U10 44.0 mm to (-5.50, 45.5)
- moved R12 43.2 mm to (-4.75, 42.8), turned to 0 degrees
- moved U8 38.9 mm to (2.50, 44.5)
- moved Q5 32.8 mm to (-6.00, 31.2)
- moved U6 30.3 mm to (58.8, 46.8)
- moved R10 28.5 mm to (-13.5, 43.0)
- moved U7 27.1 mm to (-13.5, 34.2), turned to -90 degrees
- moved D324 27.0 mm to (-2.00, 40.5), turned to 90 degrees
- moved D323 24.0 mm to (-8.50, 35.2), turned to 90 degrees
- moved D322 21.2 mm to (-0.75, 45.0), turned to -90 degrees
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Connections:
- R12 pad 2: /power/~{CHG} -> ~{CHG}
- R73 pad 1: /3V3 -> +3V3
- U1 pad 23: +3V3 -> +5V
- U2 pad 23: +3V3 -> +5V
- U3 pad 23: +3V3 -> +5V
- U4 pad 23: +3V3 -> +5V
- U4 pad 28: +3V3 -> +5V
- U5 pad 10: PWMY0 -> PWMY1
- U5 pad 11: PWMW0 -> PWMW1
- U5 pad 12: unconnected-(U5-Pad12) -> PWMY0
- U5 pad 13: unconnected-(U5-Pad13) -> PWMW0
- U5 pad 6: unconnected-(U5-Pad6) -> BAT_MEAS
- U5 pad 7: unconnected-(U5-Pad7) -> ~{CHG}
- U5 pad 8: PWMY1 -> HAS_12V
- U5 pad 9: PWMW1 -> unconnected-(U5-Pad9)
- U7 pad 1: +12V -> GND
- U7 pad 2: GND -> Net-(D323-Pad2)
- U7 pad 3: Net-(D323-Pad2) -> +12V
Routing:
- net +5V: track 0.00 -> 165.7 mm
- net VBUS: track 0.00 -> 79.5 mm, vias 0 -> 3
- net D+: track 0.00 -> 67.8 mm
- net D-: track 0.00 -> 66.1 mm
- net PWMW0: track 0.00 -> 62.7 mm, vias 0 -> 2
- net PWMY0: track 0.00 -> 58.6 mm, vias 0 -> 2
- net PWMW1: track 0.00 -> 54.5 mm, vias 0 -> 2
- net PWMY1: track 0.00 -> 50.4 mm, vias 0 -> 2
- net HAS_12V: track 0.00 -> 46.8 mm, vias 0 -> 3
- net ~{CHG}: track 0.00 -> 41.7 mm, vias 0 -> 2
- net +BATT: track 0.00 -> 40.6 mm, vias 0 -> 2
- net +3V3: track 0.00 -> 35.1 mm, vias 0 -> 2
- net GND: track 34.4 -> 62.3 mm, vias 2 -> 3
- net BAT_MEAS: track 0.00 -> 9.00 mm
- net Net-(D323-Pad2): track 0.00 -> 7.07 mm
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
